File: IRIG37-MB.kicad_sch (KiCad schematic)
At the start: 1 part

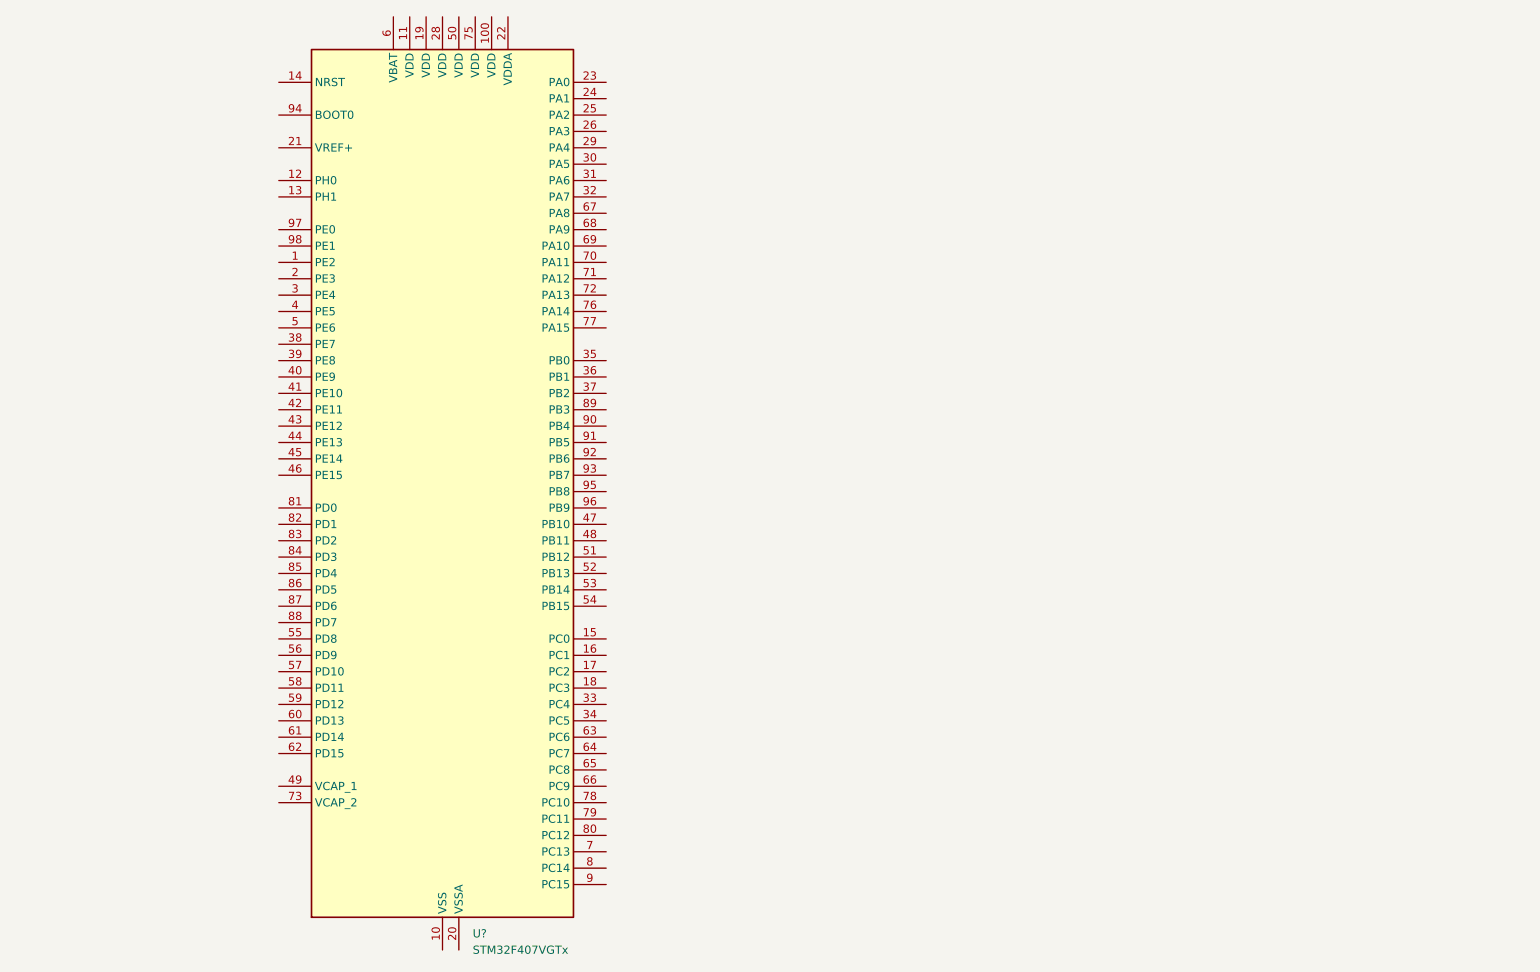
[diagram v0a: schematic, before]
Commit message: feat(sch): integrate connector sheets into main schematic
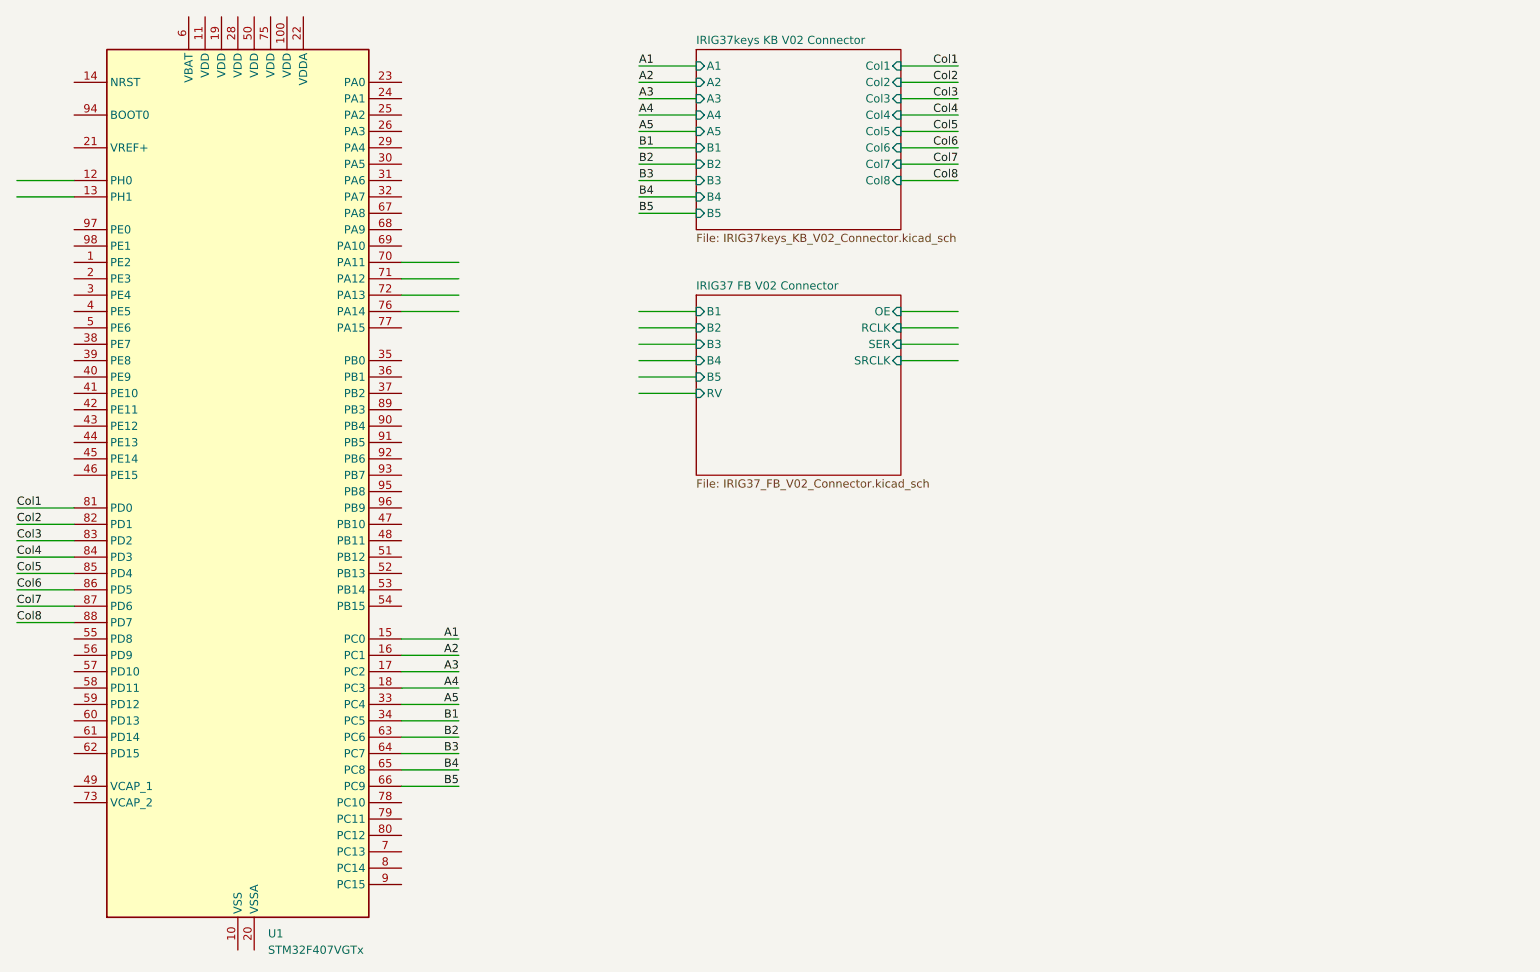
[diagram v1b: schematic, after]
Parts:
- gave numbers to parts that had none: 1
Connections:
- net A1: now reaches U1.15 (PC0)
- net A2: now reaches U1.16 (PC1)
- net A3: now reaches U1.17 (PC2)
- net A4: now reaches U1.18 (PC3)
- net A5: now reaches U1.33 (PC4)
- net B1: now reaches U1.34 (PC5)
- net B2: now reaches U1.63 (PC6)
- net B3: now reaches U1.64 (PC7)
- net B4: now reaches U1.65 (PC8)
- net B5: now reaches U1.66 (PC9)
- net Col1: now reaches U1.81 (PD0)
- net Col2: now reaches U1.82 (PD1)
- net Col3: now reaches U1.83 (PD2)
- net Col4: now reaches U1.84 (PD3)
- net Col5: now reaches U1.85 (PD4)
- net Col6: now reaches U1.86 (PD5)
- net Col7: now reaches U1.87 (PD6)
- net Col8: now reaches U1.88 (PD7)
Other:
- added sheet IRIG37 FB V02 Connector (IRIG37_FB_V02_Connector.kicad_sch)
- added sheet IRIG37keys KB V02 Connector (IRIG37keys_KB_V02_Connector.kicad_sch)
- moved on the sheet: U1

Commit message: chore(erc): mark unused pins no-connect; add pin map note
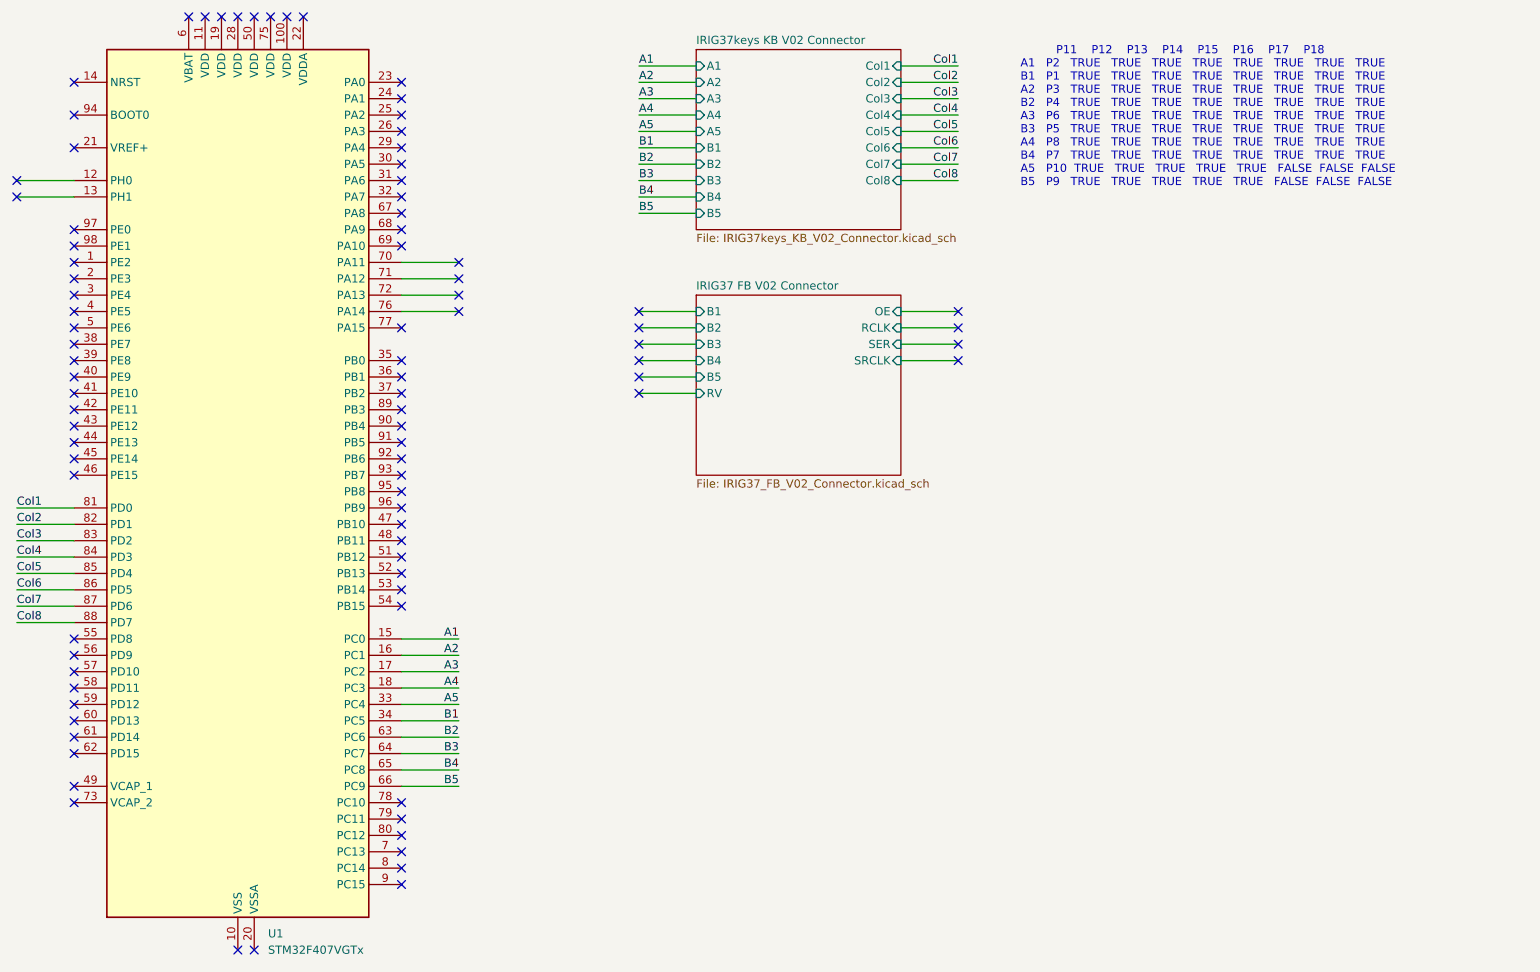
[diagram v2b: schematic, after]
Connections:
- no-connect marks 0 -> 89
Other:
- note added: "P11 P12 P13 P14 P15 P16 P17 P18 A1 P2 TRUE TRUE TRUE TRUE TRUE TRUE TRUE TRUE B1 P1 TRUE TRUE TRUE TRUE TRUE TRUE TRUE TRUE A2 P3 TRUE TRUE TRUE TRUE TRUE TRUE TRUE TRUE B2 P4 TRUE TRUE TRUE TRUE TRUE TRUE TRUE TRUE A3 P6 TRUE TRUE TRUE TRUE TRUE TRUE TRUE TRUE B3 P5 TRUE TRUE TRUE TRUE TRUE TRUE TRUE TRUE A4 P8 TRUE TRUE TRUE TRUE TRUE TRUE TRUE TRUE B4 P7 TRUE TRUE TRUE TRUE TRUE TRUE TRUE TRUE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"
